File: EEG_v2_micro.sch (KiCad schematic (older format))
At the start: 34 parts, among them SW2 SW_PUSH, SW3 SW_PUSH, U6 CC2540, U7 2450BM15A0002E, X1 32-MHz, X2 32-MHz

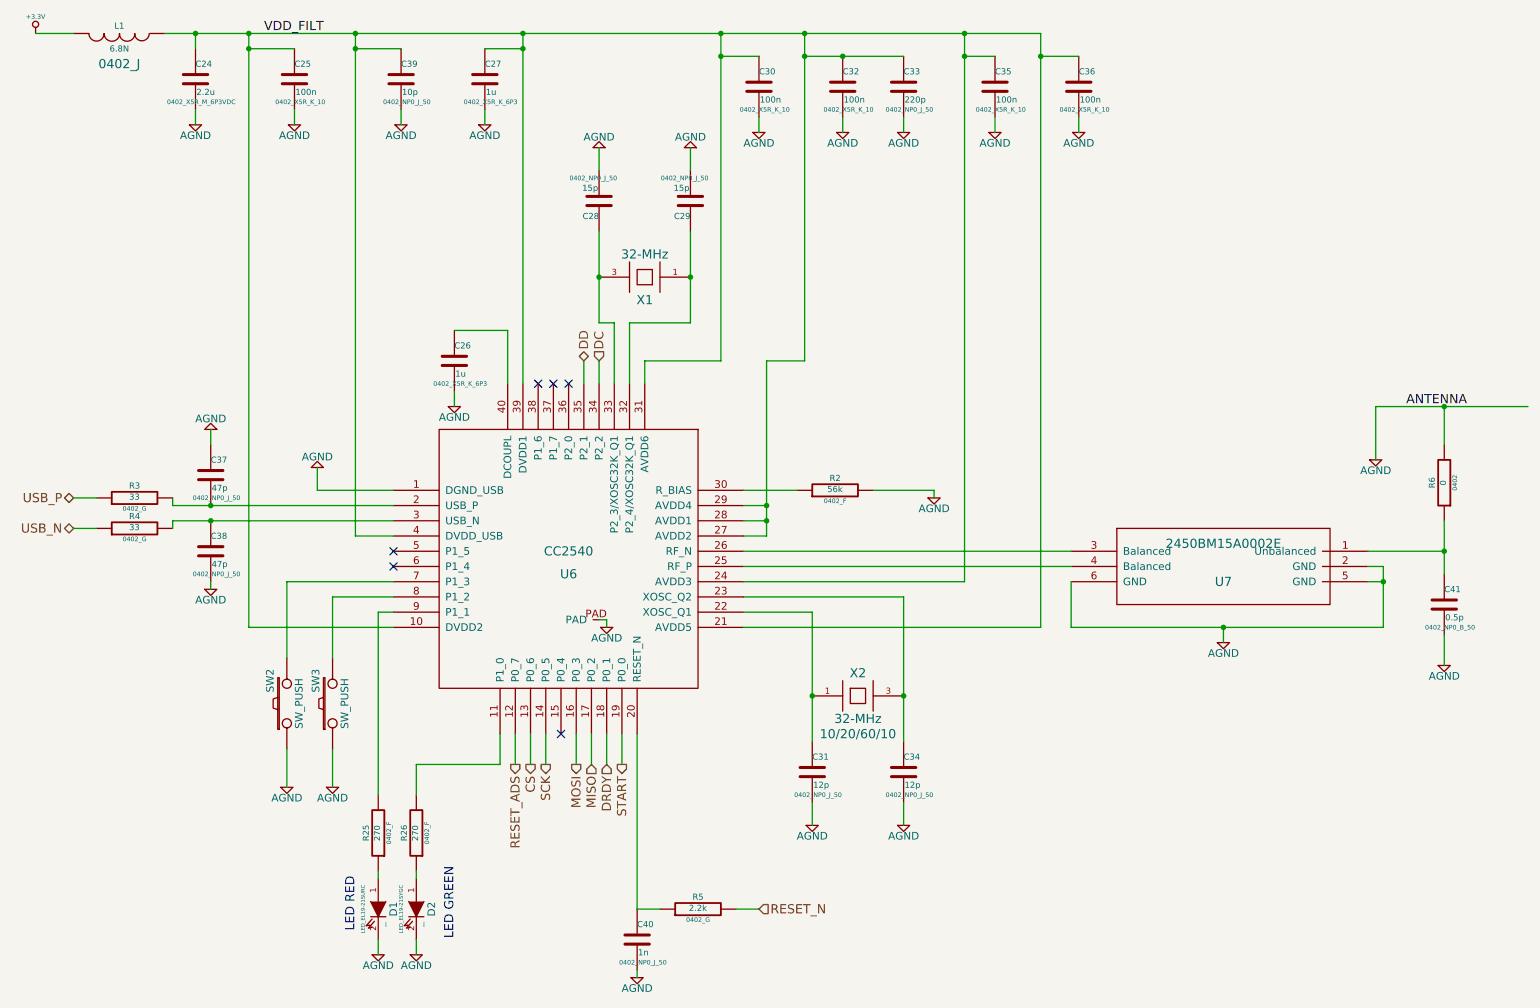
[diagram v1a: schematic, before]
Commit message: Added footprints to connectors. Changed usb A to usb micro B
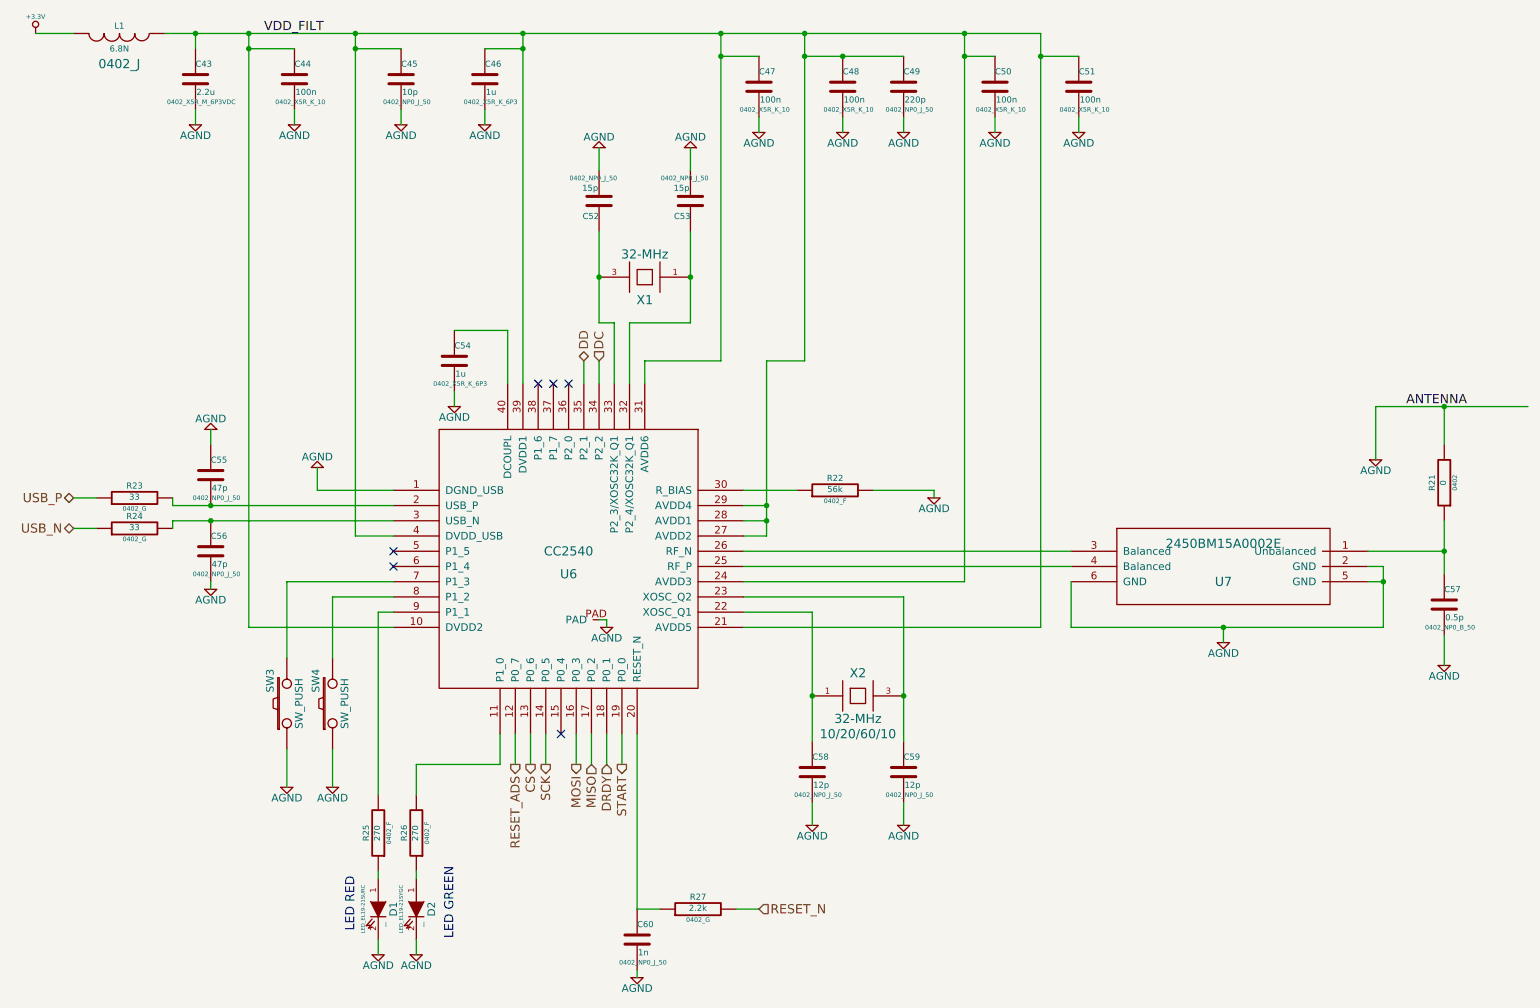
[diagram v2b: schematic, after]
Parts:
- renumbered C24 to C43, C25 to C44, C39 to C45, C27 to C46, C30 to C47, C32 to C48, C33 to C49, C35 to C50, C36 to C51, C28 to C52, C29 to C53, C26 to C54, C37 to C55, C38 to C56, C41 to C57, C31 to C58, C34 to C59, C40 to C60, R6 to R21, R2 to R22, R3 to R23, R4 to R24, R5 to R27, SW2 to SW3, SW3 to SW4
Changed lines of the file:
@@
 $EndComp
 $Comp
-L C C26
+L C C54
 U 1 1 54B4DAF5
 P 3400 3550
-F 0 "C26" H 3400 3650 40  0000 L CNN
+F 0 "C54" H 3400 3650 40  0000 L CNN
 F 1 "1u" H 3406 3465 40  0000 L CNN
 F 2 "0402_X5R_K_6P3" H 3438 3400 30  0000 C CNN
@@
 $EndComp
 $Comp
-L R R2
+L R R22
 U 1 1 54B4DE9D
 P 5900 4400
-F 0 "R2" V 5980 4400 40  0000 C CNN
+F 0 "R22" V 5980 4400 40  0000 C CNN
 F 1 "56k" V 5907 4401 40  0000 C CNN
 F 2 "0402_F" V 5830 4400 30  0000 C CNN
@@
 $EndComp
 $Comp
-L C C31
+L C C58
 U 1 1 54B4E0D9
 P 5750 6250
-F 0 "C31" H 5750 6350 40  0000 L CNN
+F 0 "C58" H 5750 6350 40  0000 L CNN
 F 1 "12p" H 5756 6165 40  0000 L CNN
 F 2 "0402_NP0_J_50" H 5788 6100 30  0000 C CNN
@@
 $EndComp
 $Comp
-L C C34
+L C C59
 U 1 1 54B4E0DF
 P 6350 6250
-F 0 "C34" H 6350 6350 40  0000 L CNN
+F 0 "C59" H 6350 6350 40  0000 L CNN
 F 1 "12p" H 6356 6165 40  0000 L CNN
 F 2 "0402_NP0_J_50" H 6388 6100 30  0000 C CNN
@@
 $EndComp
 $Comp
-L C C29
+L C C53
 U 1 1 54B4E361
 P 4950 2500
-F 0 "C29" H 4950 2600 40  0000 L CNN
+F 0 "C53" H 4950 2600 40  0000 L CNN
 F 1 "15p" H 4956 2415 40  0000 L CNN
 F 2 "0402_NP0_J_50" H 4988 2350 30  0000 C CNN
@@
 $EndComp
 $Comp
-L C C28
+L C C52
 U 1 1 54B4E367
 P 4350 2500
-F 0 "C28" H 4350 2600 40  0000 L CNN
+F 0 "C52" H 4350 2600 40  0000 L CNN
 F 1 "15p" H 4356 2415 40  0000 L CNN
 F 2 "0402_NP0_J_50" H 4388 2350 30  0000 C CNN
@@
 SCK
 $Comp
-L C C25
+L C C44
 U 1 1 54B6FDC9
 P 2350 1700
-F 0 "C25" H 2350 1800 40  0000 L CNN
+F 0 "C44" H 2350 1800 40  0000 L CNN
 F 1 "100n" H 2356 1615 40  0000 L CNN
 F 2 "0402_X5R_K_10" H 2388 1550 30  0000 C CNN
@@
 $EndComp
 $Comp
-L C C24
+L C C43
 U 1 1 54B6FDD8
 P 1700 1700
-F 0 "C24" H 1700 1800 40  0000 L CNN
+F 0 "C43" H 1700 1800 40  0000 L CNN
 F 1 "2.2u" H 1706 1615 40  0000 L CNN
 F 2 "0402_X5R_M_6P3VDC" H 1738 1550 30  0000 C CNN
@@
 $EndComp
 $Comp
-L C C27
+L C C46
 U 1 1 54B7039D
 P 3600 1700
-F 0 "C27" H 3600 1800 40  0000 L CNN
+F 0 "C46" H 3600 1800 40  0000 L CNN
 F 1 "1u" H 3606 1615 40  0000 L CNN
 F 2 "0402_X5R_K_6P3" H 3638 1550 30  0000 C CNN
@@
 $EndComp
 $Comp
-L C C30
+L C C47
 U 1 1 54B708C7
 P 5400 1750
-F 0 "C30" H 5400 1850 40  0000 L CNN
+F 0 "C47" H 5400 1850 40  0000 L CNN
 F 1 "100n" H 5406 1665 40  0000 L CNN
 F 2 "0402_X5R_K_10" H 5438 1600 30  0000 C CNN
@@
 $EndComp
 $Comp
-L C C32
+L C C48
 U 1 1 54B70B01
 P 5950 1750
-F 0 "C32" H 5950 1850 40  0000 L CNN
+F 0 "C48" H 5950 1850 40  0000 L CNN
 F 1 "100n" H 5956 1665 40  0000 L CNN
 F 2 "0402_X5R_K_10" H 5988 1600 30  0000 C CNN
@@
 $EndComp
 $Comp
-L C C33
+L C C49
 U 1 1 54B70B0E
 P 6350 1750
-F 0 "C33" H 6350 1850 40  0000 L CNN
+F 0 "C49" H 6350 1850 40  0000 L CNN
 F 1 "220p" H 6356 1665 40  0000 L CNN
 F 2 "0402_NP0_J_50" H 6388 1600 30  0000 C CNN
@@
 $EndComp
 $Comp
-L C C35
+L C C50
 U 1 1 54B70FFF
 P 6950 1750
-F 0 "C35" H 6950 1850 40  0000 L CNN
+F 0 "C50" H 6950 1850 40  0000 L CNN
 F 1 "100n" H 6956 1665 40  0000 L CNN
 F 2 "0402_X5R_K_10" H 6988 1600 30  0000 C CNN
@@
 $EndComp
 $Comp
-L C C36
+L C C51
 U 1 1 54B7105B
 P 7500 1750
-F 0 "C36" H 7500 1850 40  0000 L CNN
+F 0 "C51" H 7500 1850 40  0000 L CNN
 F 1 "100n" H 7506 1665 40  0000 L CNN
 F 2 "0402_X5R_K_10" H 7538 1600 30  0000 C CNN
@@
 RESET_ADS
 $Comp
-L C C39
+L C C45
 U 1 1 54B75300
 P 3050 1700
-F 0 "C39" H 3050 1800 40  0000 L CNN
+F 0 "C45" H 3050 1800 40  0000 L CNN
 F 1 "10p" H 3056 1615 40  0000 L CNN
 F 2 "0402_NP0_J_50" H 3088 1550 30  0000 C CNN
@@
 Connection ~ 2750 1500
 $Comp
-L R R3
+L R R23
 U 1 1 54B7579A
 P 1300 4450
-F 0 "R3" V 1380 4450 40  0000 C CNN
+F 0 "R23" V 1380 4450 40  0000 C CNN
 F 1 "33" V 1307 4451 40  0000 C CNN
 F 2 "0402_G" V 1230 4450 30  0000 C CNN
@@
 $EndComp
 $Comp
-L R R4
+L R R24
 U 1 1 54B757A0
 P 1300 4650
-F 0 "R4" V 1380 4650 40  0000 C CNN
+F 0 "R24" V 1380 4650 40  0000 C CNN
 F 1 "33" V 1307 4651 40  0000 C CNN
 F 2 "0402_G" V 1230 4650 30  0000 C CNN
@@
 	1050 4650 900  4650
 $Comp
-L C C38
+L C C56
 U 1 1 54B75968
 P 1800 4800
-F 0 "C38" H 1800 4900 40  0000 L CNN
+F 0 "C56" H 1800 4900 40  0000 L CNN
 F 1 "47p" H 1806 4715 40  0000 L CNN
 F 2 "0402_NP0_J_50" H 1838 4650 30  0000 C CNN
@@
 $EndComp
 $Comp
-L C C37
+L C C55
 U 1 1 54B75989
 P 1800 4300
-F 0 "C37" H 1800 4400 40  0000 L CNN
+F 0 "C55" H 1800 4400 40  0000 L CNN
 F 1 "47p" H 1806 4215 40  0000 L CNN
 F 2 "0402_NP0_J_50" H 1838 4150 30  0000 C CNN
@@
 NoConn ~ 4100 6000
 $Comp
-L C C40
+L C C60
 U 1 1 54C2E982
 P 4600 7350
-F 0 "C40" H 4600 7450 40  0000 L CNN
+F 0 "C60" H 4600 7450 40  0000 L CNN
 F 1 "1n" H 4606 7265 40  0000 L CNN
 F 2 "0402_NP0_J_50" H 4638 7200 30  0000 C CNN
@@
 $EndComp
 $Comp
-L R R5
+L R R27
 U 1 1 54C2EA77
 P 5000 7150
-F 0 "R5" V 5080 7150 40  0000 C CNN
+F 0 "R27" V 5080 7150 40  0000 C CNN
 F 1 "2.2k" V 5007 7151 40  0000 C CNN
 F 2 "0402_G" V 4930 7150 30  0000 C CNN
@@
 	5250 7150 5400 7150
 $Comp
-L C C41
+L C C57
 U 1 1 54C2ECFD
 P 9900 5150
-F 0 "C41" H 9900 5250 40  0000 L CNN
+F 0 "C57" H 9900 5250 40  0000 L CNN
 F 1 "0.5p" H 9906 5065 40  0000 L CNN
 F 2 "0402_NP0_B_50" H 9938 5000 30  0000 C CNN
@@
 Connection ~ 9900 4800
 $Comp
-L R R6
+L R R21
 U 1 1 54C2ED93
 P 9900 4350
-F 0 "R6" V 9980 4350 40  0000 C CNN
+F 0 "R21" V 9980 4350 40  0000 C CNN
 F 1 "0" V 9907 4351 40  0000 C CNN
 F 2 "0402" V 9830 4350 30  0000 C CNN
@@
 	3750 3350 3400 3350
 $Comp
-L SW_PUSH SW2
+L SW_PUSH SW3
 U 1 1 54CBF5D1
 P 2300 5800
-F 0 "SW2" H 2450 5910 50  0000 C CNN
+F 0 "SW3" H 2450 5910 50  0000 C CNN
 F 1 "SW_PUSH" H 2300 5720 50  0000 C CNN
 F 2 "~" H 2300 5800 60  0000 C CNN
@@
 	3150 6200 3700 6200
 $Comp
-L SW_PUSH SW3
+L SW_PUSH SW4
 U 1 1 54CBFC84
 P 2600 5800
-F 0 "SW3" H 2750 5910 50  0000 C CNN
+F 0 "SW4" H 2750 5910 50  0000 C CNN
 F 1 "SW_PUSH" H 2600 5720 50  0000 C CNN
 F 2 "~" H 2600 5800 60  0000 C CNN

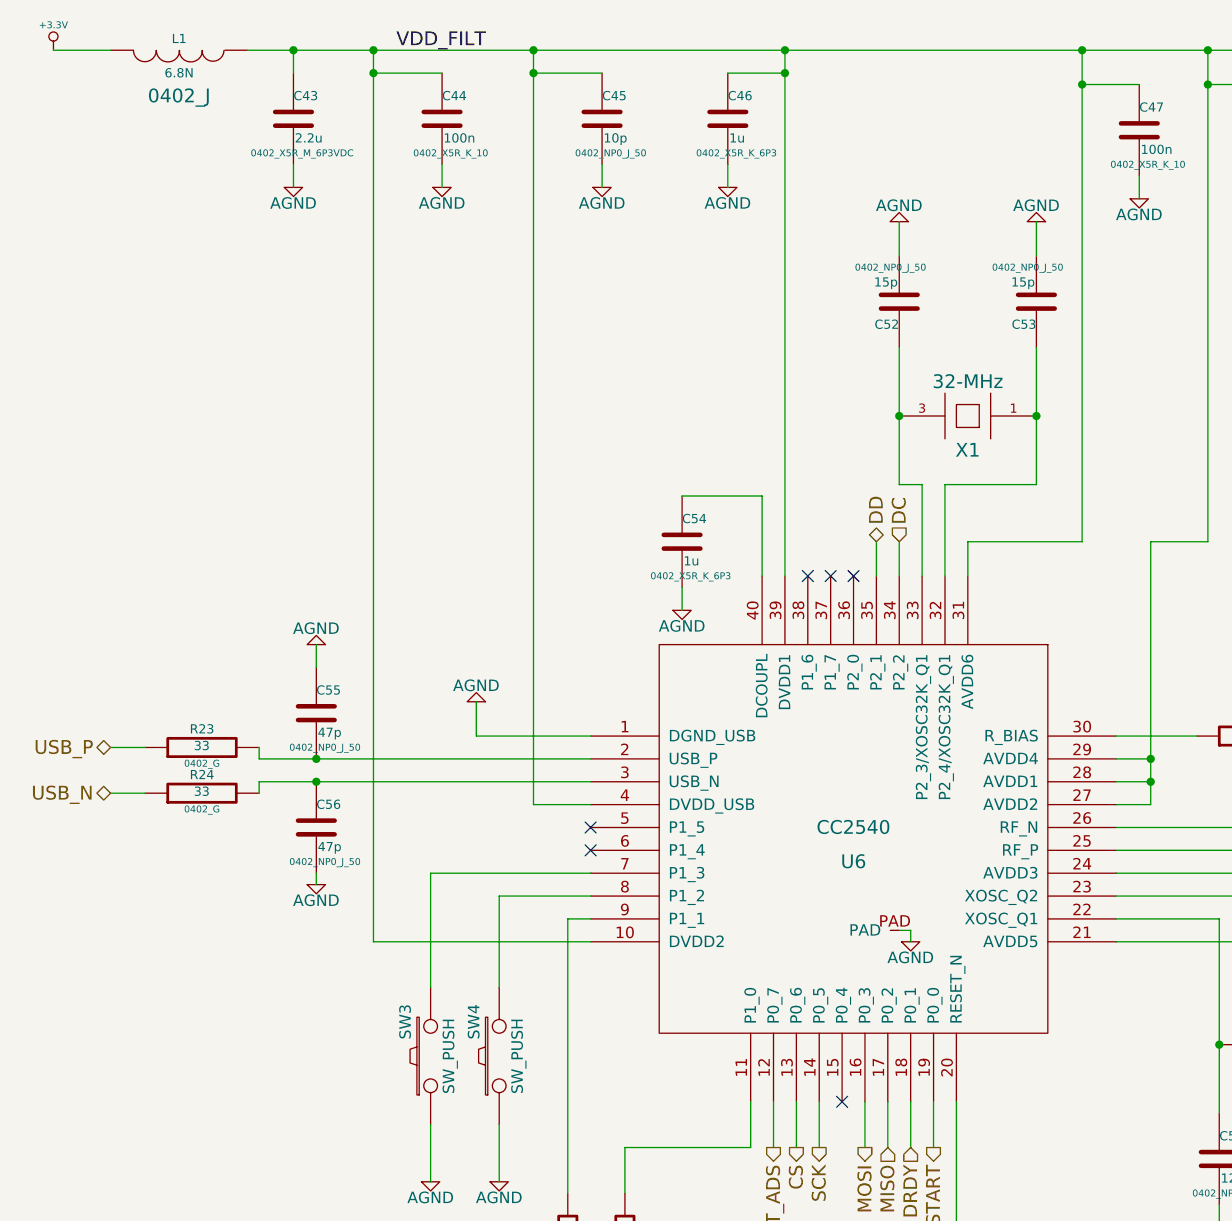
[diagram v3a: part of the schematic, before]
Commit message: Add footprints for tactile switches
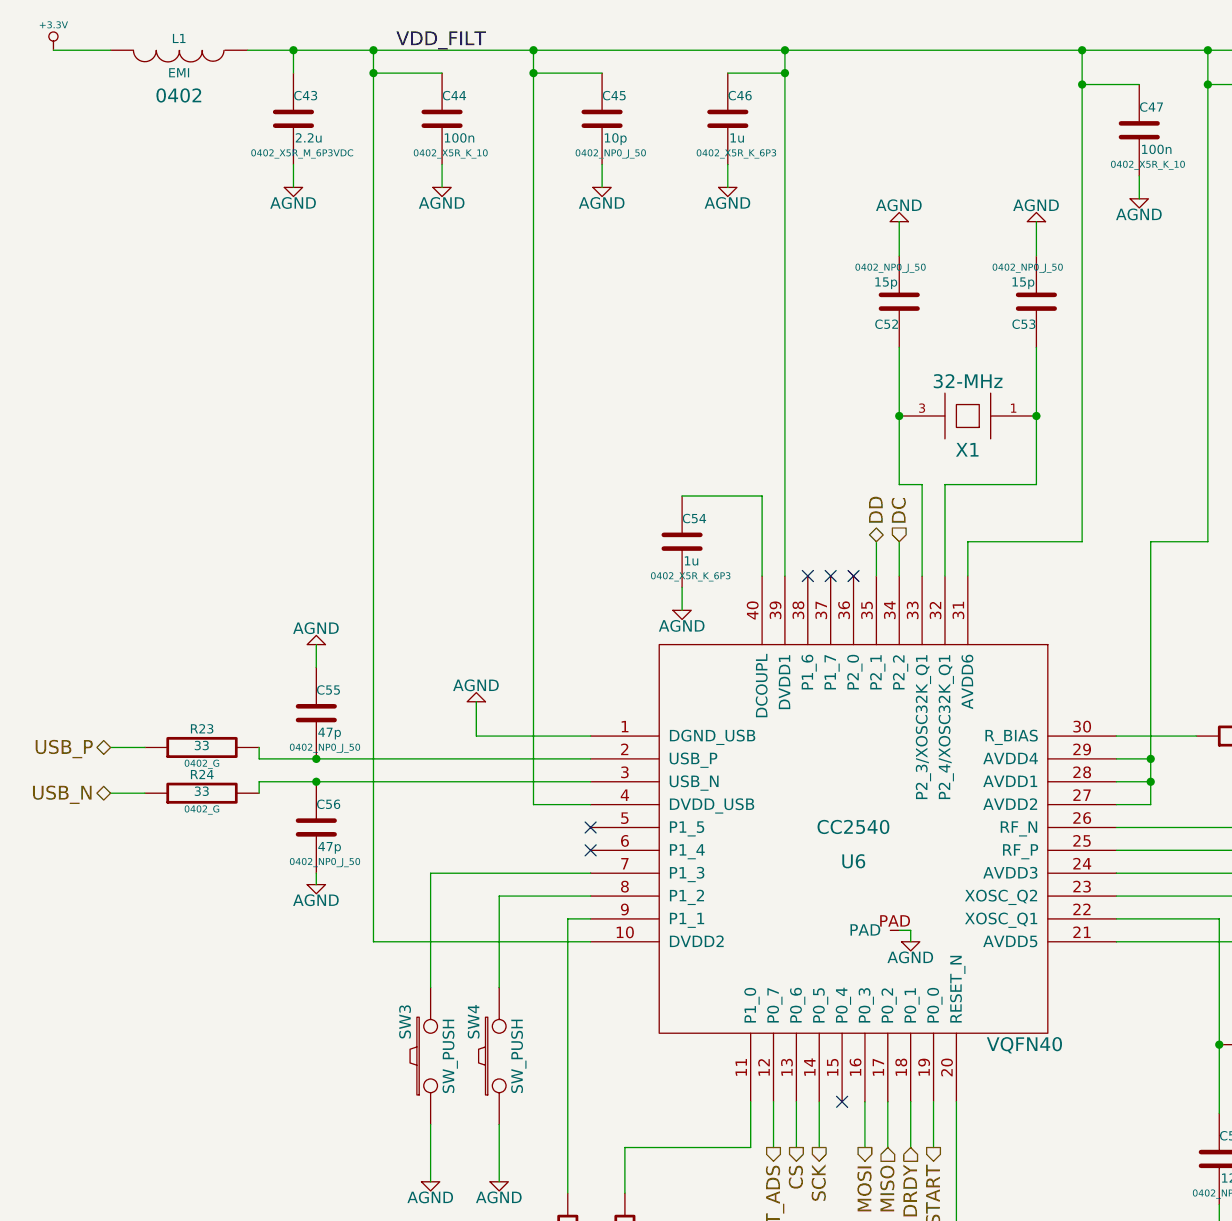
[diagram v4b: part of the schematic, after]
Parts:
- L1: value 6.8N -> EMI; footprint 0402_J -> 0402
- SW3, SW4: footprint ~ -> Thru 1825910
- U6: footprint (none) -> VQFN40
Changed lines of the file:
@@
 F 0 "U6" H 4150 4750 60  0000 C CNN
 F 1 "CC2540" H 4150 4900 60  0000 C CNN
-F 2 "" H 4150 4900 60  0000 C CNN
+F 2 "VQFN40" H 4900 3950 60  0000 C CNN
 F 3 "" H 4150 4900 60  0000 C CNN
 	1    4150 4850
@@
 P 1200 1400
 F 0 "L1" V 1150 1400 40  0000 C CNN
-F 1 "6.8N" V 1300 1400 40  0000 C CNN
-F 2 "0402_J" V 1400 1400 60  0000 C CNN
+F 1 "EMI" V 1300 1400 40  0000 C CNN
+F 2 "0402" V 1400 1400 60  0000 C CNN
 F 3 "~" H 1200 1400 60  0000 C CNN
 	1    1200 1400
@@
 F 0 "SW3" H 2450 5910 50  0000 C CNN
 F 1 "SW_PUSH" H 2300 5720 50  0000 C CNN
-F 2 "~" H 2300 5800 60  0000 C CNN
+F 2 "Thru 1825910" H 2300 5800 60  0001 C CNN
 F 3 "~" H 2300 5800 60  0000 C CNN
 	1    2300 5800
@@
 F 0 "SW4" H 2750 5910 50  0000 C CNN
 F 1 "SW_PUSH" H 2600 5720 50  0000 C CNN
-F 2 "~" H 2600 5800 60  0000 C CNN
+F 2 "Thru 1825910" H 2600 5800 60  0001 C CNN
 F 3 "~" H 2600 5800 60  0000 C CNN
 	1    2600 5800

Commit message: Add balun datasheet
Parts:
- U7: footprint ~ -> 2450BM15A0002E
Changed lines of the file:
@@
 F 0 "U7" H 8450 4800 60  0000 C CNN
 F 1 "2450BM15A0002E" H 8450 5050 60  0000 C CNN
-F 2 "~" H 8450 4850 60  0000 C CNN
+F 2 "2450BM15A0002E" H 8450 4600 60  0000 C CNN
 F 3 "~" H 8450 4850 60  0000 C CNN
 	1    8450 4900

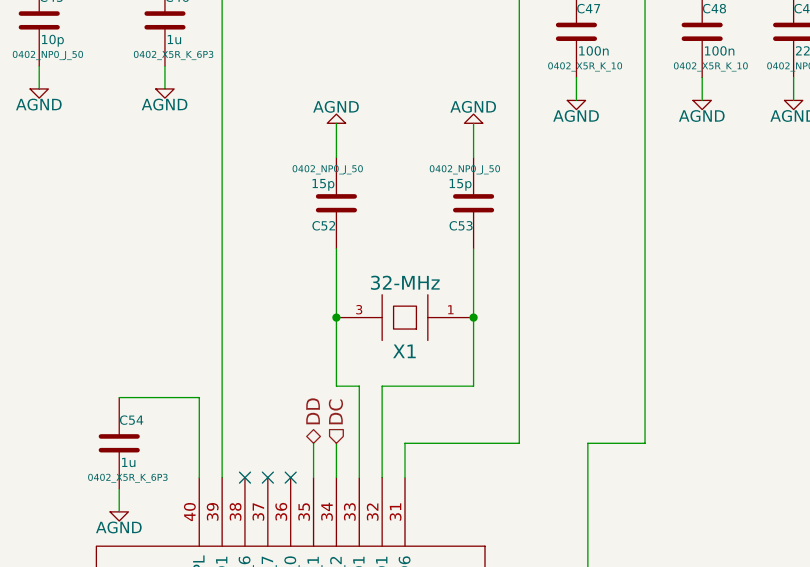
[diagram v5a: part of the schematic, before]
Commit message: Correct 32k crystal
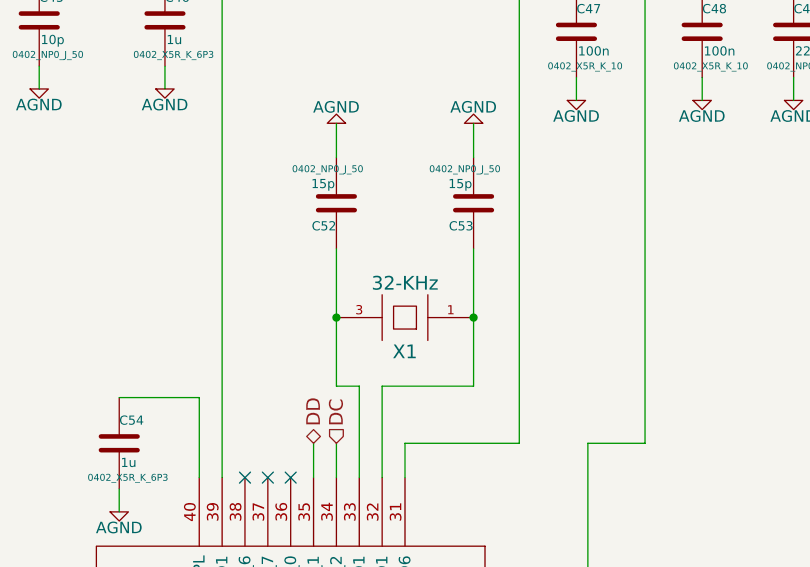
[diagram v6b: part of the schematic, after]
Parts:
- X1: value 32-MHz -> 32-KHz
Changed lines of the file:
@@
 P 4650 3000
 F 0 "X1" H 4650 3150 60  0000 C CNN
-F 1 "32-MHz" H 4650 2850 60  0000 C CNN
+F 1 "32-KHz" H 4650 2850 60  0000 C CNN
 F 2 "~" H 4650 3000 60  0000 C CNN
 F 3 "~" H 4650 3000 60  0000 C CNN
